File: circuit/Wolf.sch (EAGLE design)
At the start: 21 parts, among them IC1 74LS595N, K1 SNES, M1 ARDUINO-NANO-3.0

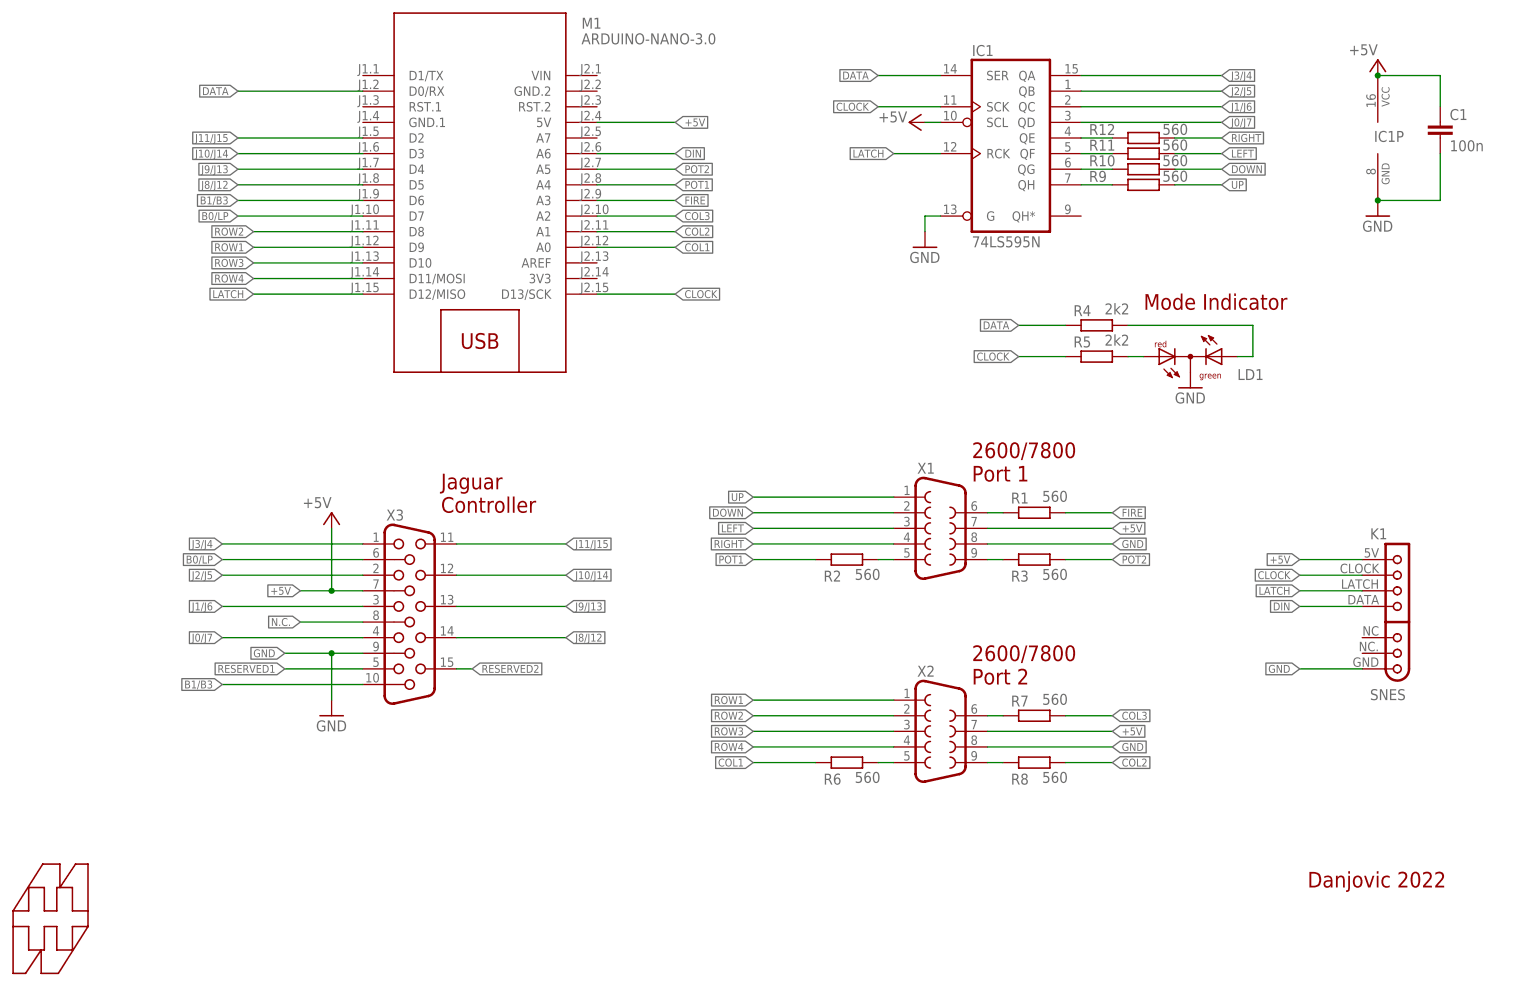
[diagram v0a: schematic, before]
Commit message: Assed savekey eeprom to the circuit
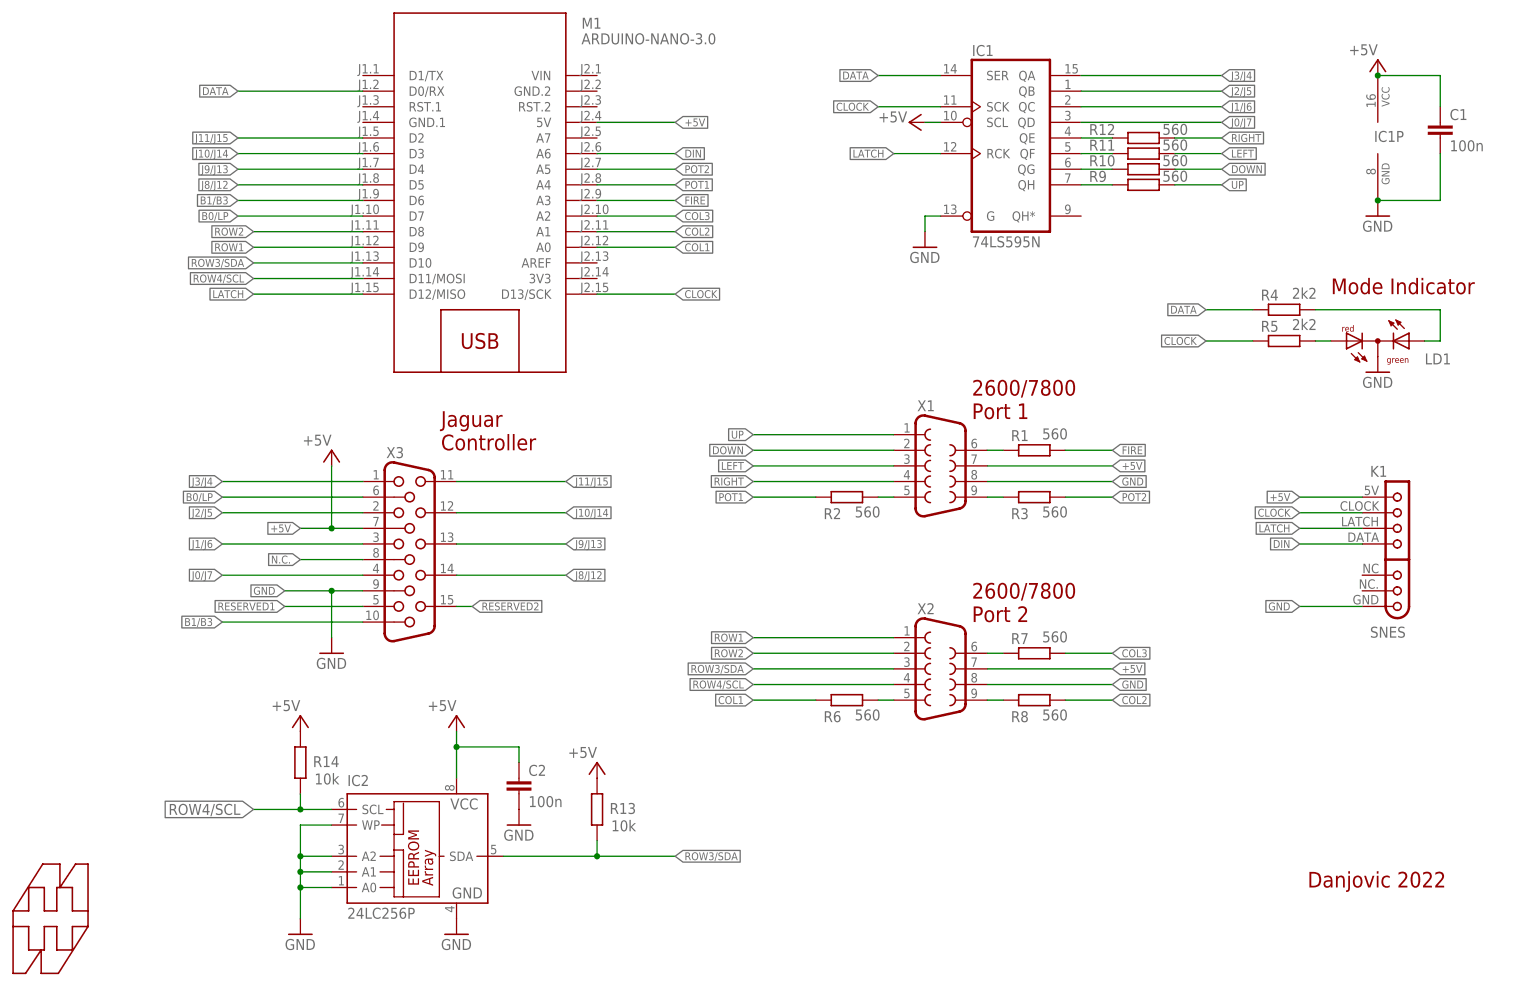
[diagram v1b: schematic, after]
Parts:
- added C2: 100n, rcl:C-EU050-024X044
- added IC2: 24LC256P, microchip:24LC256P
- added R13, R14: 10k, rcl:R-EU_0204/7
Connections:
- removed net ROW3: M1.D10, X2.3
- removed net ROW4: M1.D11/MOSI, X2.4
- new net ROW3/SDA: IC2.SDA, M1.D10, R13.1, X2.3
- new net ROW4/SCL: IC2.SCL, M1.D11/MOSI, R14.1, X2.4
- net +5V: now also C2.1, IC2.VCC, R13.2, R14.2
- net GND: now also C2.2, IC2.A0, IC2.A1, IC2.A2, IC2.GND, IC2.WP
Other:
- moved on the sheet: K1, LD1, R1, R2, R3, R4, R5, R6, R7, R8, X1, X2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

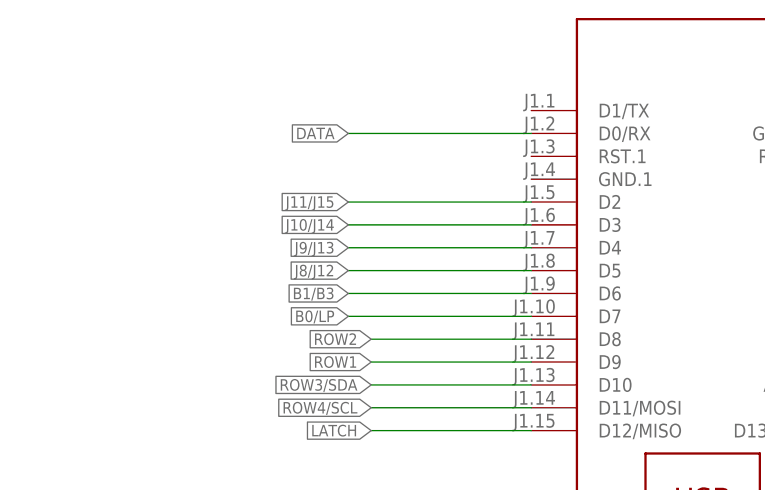
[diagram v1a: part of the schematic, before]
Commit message: Added missing GND connection
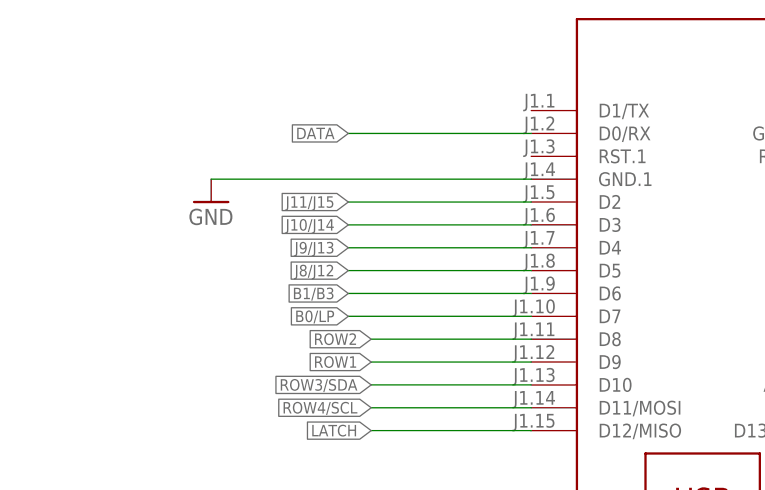
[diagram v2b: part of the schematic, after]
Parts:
- X1, X2: device con-subd:F09H -> con-subd:F09HP
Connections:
- net GND: now also M1.GND.1
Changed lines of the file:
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@@
 <parts>
 <part name="X3" library="con-subd" deviceset="HF15" device="H"/>
-<part name="X1" library="con-subd" deviceset="F09" device="H"/>
-<part name="X2" library="con-subd" deviceset="F09" device="H"/>
+<part name="X1" library="con-subd" deviceset="F09" device="HP"/>
+<part name="X2" library="con-subd" deviceset="F09" device="HP"/>
 <part name="M1" library="diy-modules" deviceset="ARDUINO-NANO-3.0" device=""/>
 <part name="K1" library="snes_breakout" deviceset="SNES" device="-R" value="SNES"/>
@@
 <part name="C2" library="rcl" deviceset="C-EU" device="050-024X044" value="100n"/>
 <part name="GND7" library="supply1" deviceset="GND" device=""/>
+<part name="GND8" library="supply1" deviceset="GND" device=""/>
 </parts>
 <sheets>
@@
 <instance part="C2" gate="G$1" x="88.9" y="38.1"/>
 <instance part="GND7" gate="1" x="88.9" y="30.48"/>
+<instance part="GND8" gate="1" x="27.94" y="142.24"/>
 </instances>
 <busses>
@@
 <pinref part="GND7" gate="1" pin="GND"/>
 </segment>
-</net>
+<segment>
+<pinref part="GND8" gate="1" pin="GND"/>
+<pinref part="M1" gate="G$1" pin="GND.1"/>
+<wire x1="63.5" y1="144.78" x2="27.94" y2="144.78" width="0.1524" layer="91"/>
+</segment>
+</net>
